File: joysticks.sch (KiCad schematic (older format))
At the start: 31 parts, among them CN4 JOY1, CN5 JOY2, U11 74LS125

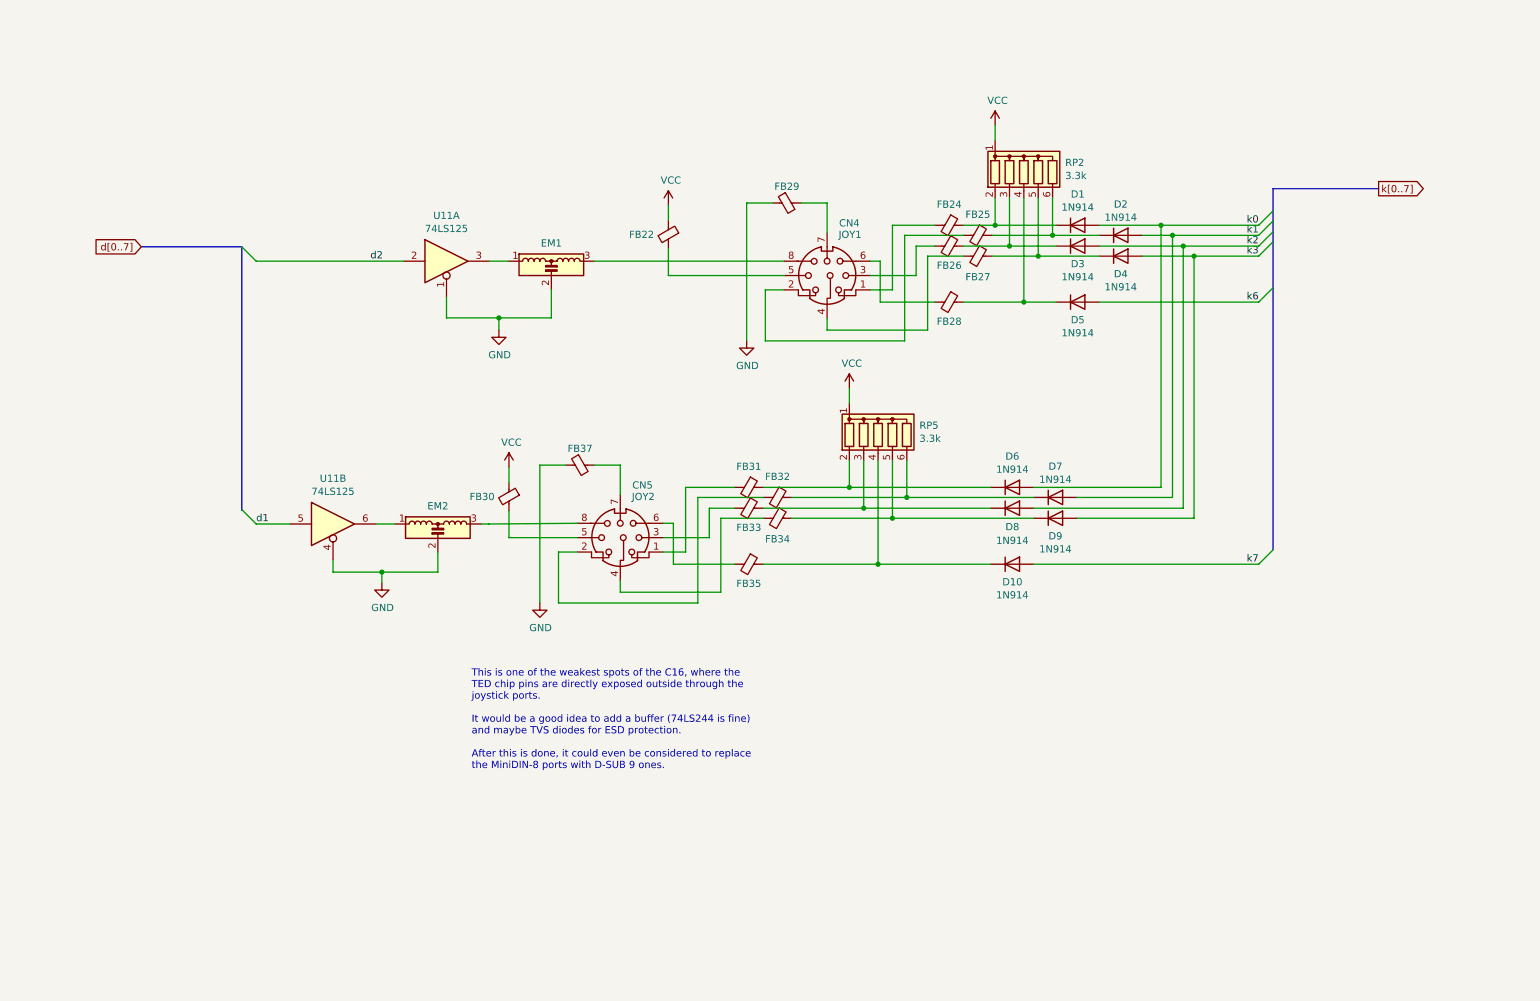
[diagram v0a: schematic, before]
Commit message: Add buffers on joystick ports - WIP
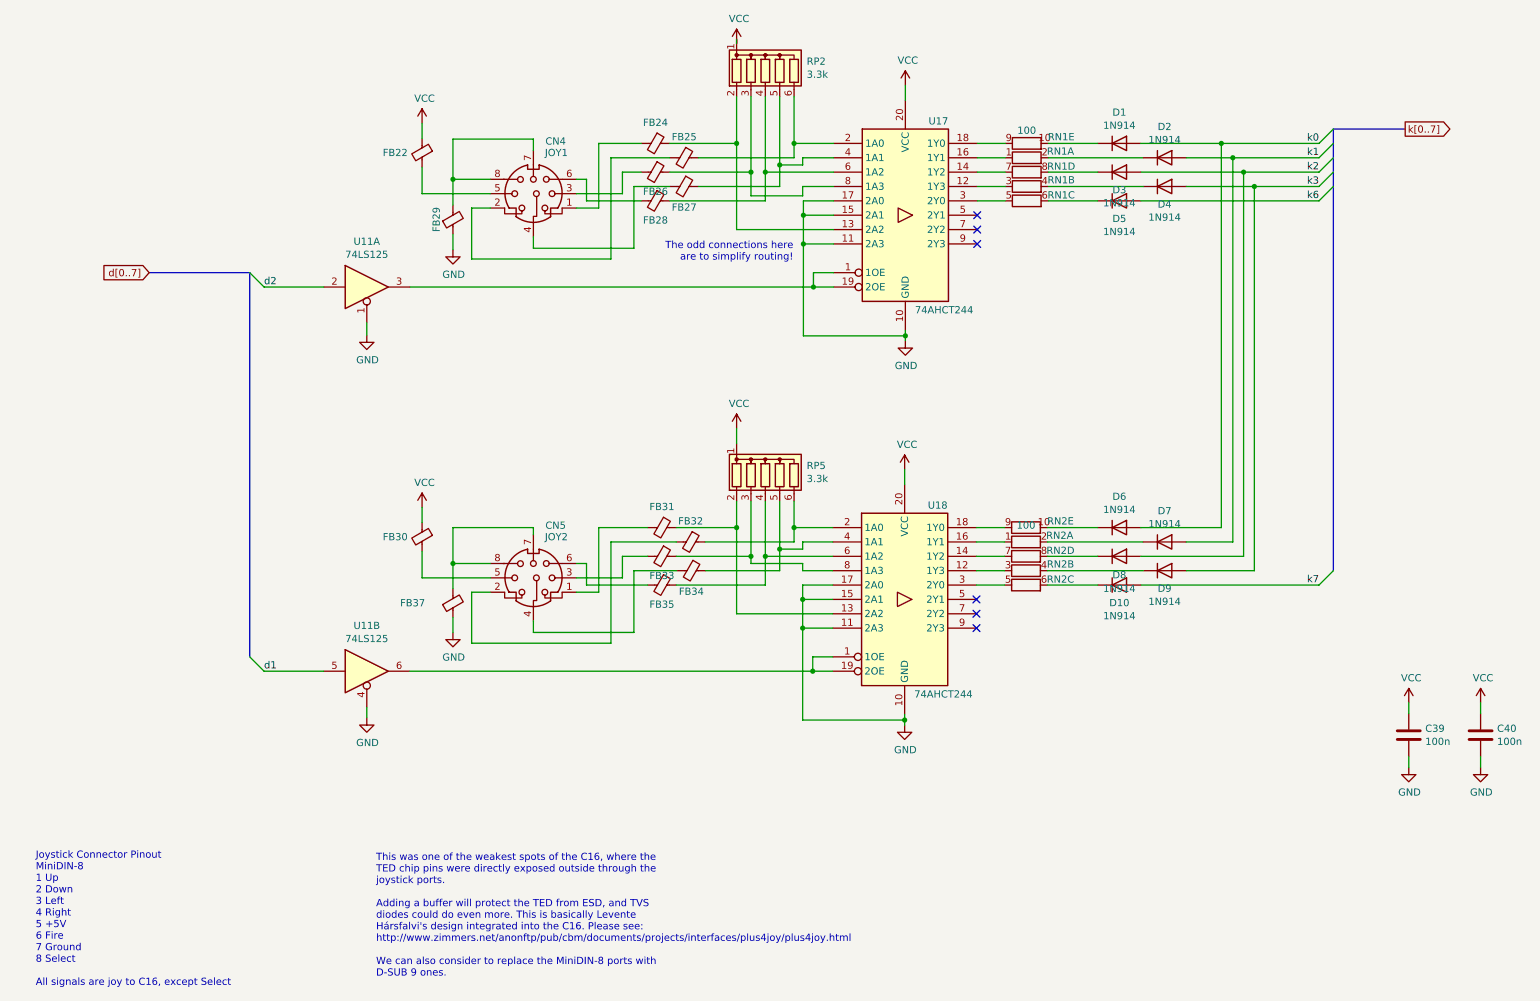
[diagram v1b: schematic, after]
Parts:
- removed EM1, EM2: EMI_Filter_LCL, LittleSixteen:EMI_Filter, symbol Device:EMI_Filter_LCL
- added C39, C40: 100n, Capacitor_THT:C_Disc_D8.0mm_W2.5mm_P5.00mm, symbol Device:C
- added RN1, RN2: 100, Resistor_THT:R_Array_SIP10, symbol Device:R_Pack05_SIP_Split
- added U17, U18: 74AHCT244, Package_DIP:DIP-20_W7.62mm_Socket_LongPads, symbol 74xx:74AHCT244
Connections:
- net GND: now also C39.2, C40.2, U17.10 (GND), U17.11 (2A3), U17.15 (2A1), U17.17 (2A0), U18.10 (GND), U18.11 (2A3), U18.15 (2A1), U18.17 (2A0)
- net VCC: now also C39.1, C40.1, U17.20 (VCC), U18.20 (VCC)
- net at CN4.7, FB29.2: now also CN4.8
- net at U11.3: now also U17.1 (1OE), U17.19 (2OE)
- net at FB24.1, RP2.2 (R1): now also U17.13 (2A2); no longer D1.1 (K)
- net at FB25.1, RP2.6 (R5): now also U17.2 (1A0); no longer D2.1 (K)
- net at FB26.1, RP2.3 (R2): now also U17.8 (1A3); no longer D3.1 (K)
- net at FB27.1, RP2.5 (R4): now also U17.4 (1A1); no longer D4.1 (K)
- net at FB28.1, RP2.4 (R3): now also U17.6 (1A2); no longer D5.1 (K)
- net at U11.6: now also U18.1 (1OE), U18.19 (2OE)
- net at CN5.8: now also CN5.7, FB37.2
- net at FB31.1, RP5.2 (R1): now also U18.13 (2A2); no longer D6.1 (K)
- net at FB32.1, RP5.6 (R5): now also U18.2 (1A0); no longer D7.1 (K)
- net at FB33.1, RP5.3 (R2): now also U18.8 (1A3); no longer D8.1 (K)
- net at FB34.1, RP5.5 (R4): now also U18.4 (1A1); no longer D9.1 (K)
- net at FB35.1, RP5.4 (R3): now also U18.6 (1A2); no longer D10.1 (K)
- new net: D1.1 (K), RN1.10 (R5.2)
- new net: D2.1 (K), RN1.2 (R1.2)
- new net: D3.1 (K), RN1.8 (R4.2)
- new net: D4.1 (K), RN1.4 (R2.2)
- new net: D5.1 (K), RN1.6 (R3.2)
- new net: D6.1 (K), RN2.10 (R5.2)
- new net: D7.1 (K), RN2.2 (R1.2)
- new net: D8.1 (K), RN2.8 (R4.2)
- new net: D9.1 (K), RN2.4 (R2.2)
- new net: D10.1 (K), RN2.6 (R3.2)
- new net: RN2.3 (R2.1), U18.12 (1Y3)
- new net: RN2.7 (R4.1), U18.14 (1Y2)
- new net: RN2.1 (R1.1), U18.16 (1Y1)
- new net: RN2.9 (R5.1), U18.18 (1Y0)
- new net: RN2.5 (R3.1), U18.3 (2Y0)
- new net: RN1.3 (R2.1), U17.12 (1Y3)
- new net: RN1.7 (R4.1), U17.14 (1Y2)
- new net: RN1.1 (R1.1), U17.16 (1Y1)
- new net: RN1.9 (R5.1), U17.18 (1Y0)
- new net: RN1.5 (R3.1), U17.3 (2Y0)
- no-connect marks 0 -> 6
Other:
- note added: "Joystick Connector Pinout\nMiniDIN-8\n1 Up\n2 Down\n3 Left\n4 Right\n5 +5V\n6 Fire\n7 Ground\n8 Select\n\nAll signals are joy to C16, except Select"
- note added: "The odd connections here\nare to simplify routing!"
- note added: "This was one of the weakest spots of the C16, where the\nTED chip pins were directly exposed outside through the\njoystick ports.\n\nAdding a buffer will protect the TED from ESD, and TVS\ndiodes could do even more. This is basically Levente\nHársfalvi's design integrated into the C16. Please see:\nhttp://www.zimmers.net/anonftp/pub/cbm/documents/projects/interfaces/plus4joy/plus4joy.html\n\nWe c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"
- note removed: "This is one of the weakest spots of the C16, where the\nTED chip pins are directly exposed outside through the\njoystick ports.\n\nIt would be a good idea to add a buffer (74LS244 is fine)\nand maybe TVS diodes for ESD protection.\n\nAfter this is done, it could even be considered to replace\nthe MiniDIN-8 ports with D-SUB 9 ones."
- moved on the sheet: CN4, CN5, D1, D10, D2, D3, D4, D5, D6, D7, D8, D9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

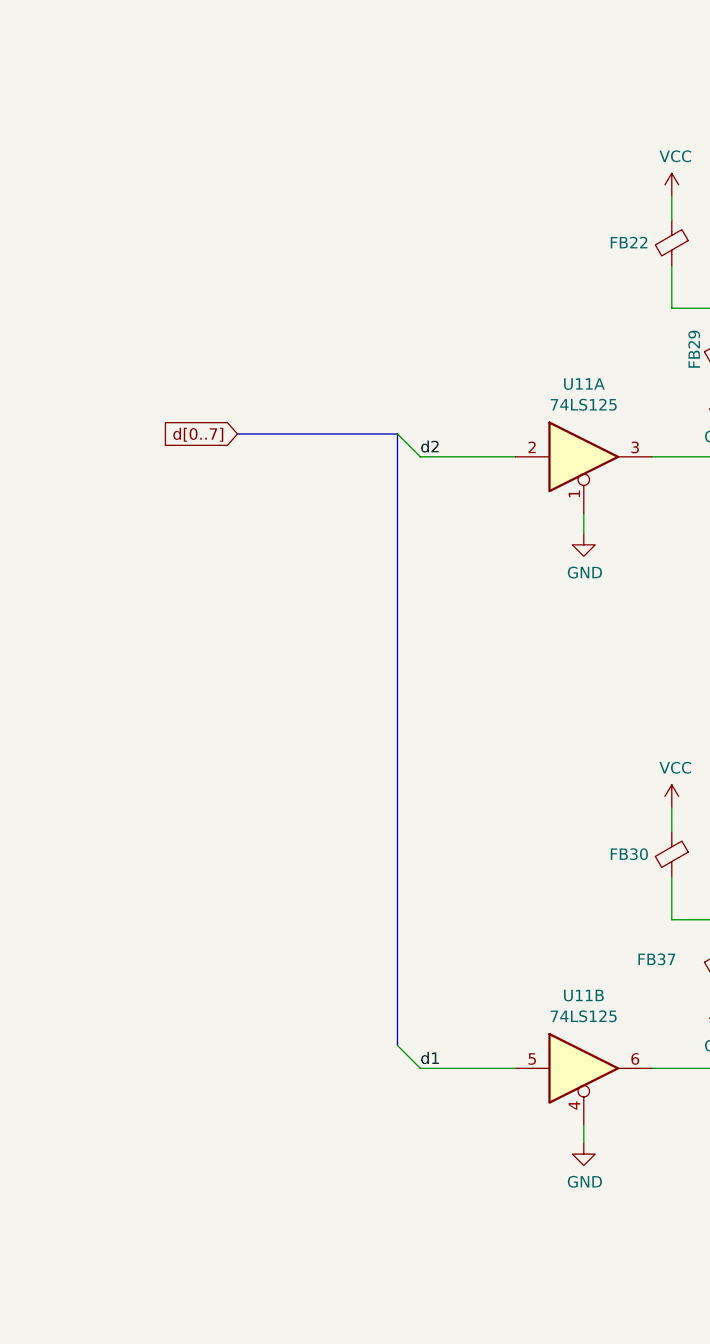
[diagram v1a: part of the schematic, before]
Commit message: Restore JD1/2
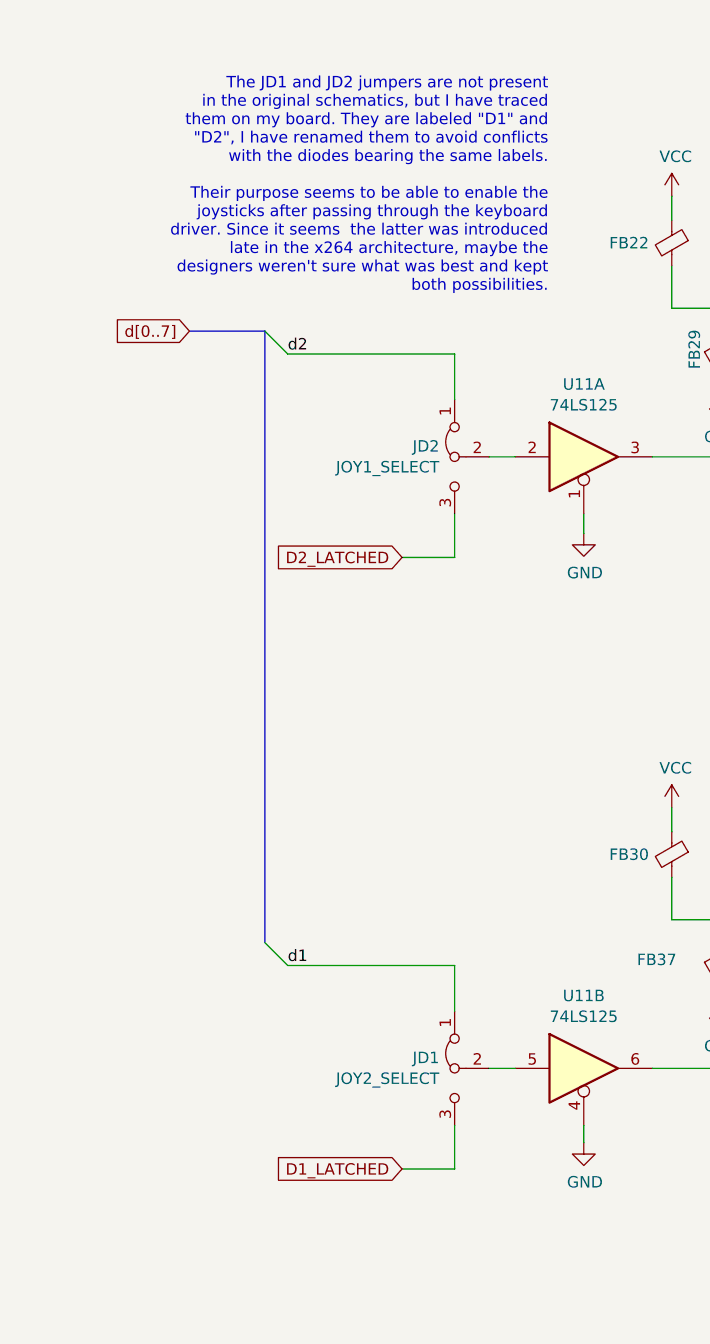
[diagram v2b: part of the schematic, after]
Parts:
- added JD1: JOY2_SELECT, LittleSixteen:SolderJumper2x, symbol Jumper:Jumper_3_Bridged12
- added JD2: JOY1_SELECT, LittleSixteen:SolderJumper2x, symbol Jumper:Jumper_3_Bridged12
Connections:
- net d1: now also JD1.1 (A); no longer U11.5
- net d2: now also JD2.1 (A); no longer U11.2
- new net: JD2.2 (C), U11.2
- new net: JD1.2 (C), U11.5
- new net D1_LATCHED: JD1.3 (B)
- new net D2_LATCHED: JD2.3 (B)
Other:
- note added: "The JD1 and JD2 jumpers are not present\nin the original schematics, but I have traced\nthem on my board. They are labeled "D1" and\n"D2", I have renamed them to avoid conflicts\nwith the diodes bearing the same labels.\n\nTheir purpose seems to be able to enable the\njoysticks after passing through the keyboard\ndriver. Since it seems the latter was introduced\nlate in the x264 architecture, may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"
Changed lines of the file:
@@
 Sheet 11 12
 Title "LittleSixteen"
-Date "2021-11-03"
+Date "2021-11-06"
 Rev "3git"
 Comp "SukkoPera"
@@
 	3255 5480 6060 5480
 Wire Wire Line
-	2240 2805 2655 2805
-Wire Wire Line
 	2955 3055 2955 3140
 Wire Wire Line
 	2955 5730 2955 5805
-Text Label 2240 5480 0    50   ~ 0
+Text Label 1660 5030 0    50   ~ 0
 d1
 Wire Wire Line
-	2240 5480 2655 5480
+	2540 5480 2655 5480
 $Comp
 L 74xx:74LS125 U11
@@
 	1    0    0    -1
 $EndComp
-Text GLabel 1440 2705 0    50   Input ~ 0
+Text GLabel 1230 2255 0    50   Input ~ 0
 d[0..7]
 Wire Bus Line
-	1440 2705 2140 2705
+	1230 2255 1560 2255
 Entry Wire Line
-	2140 5380 2240 5480
+	1560 4930 1660 5030
 Entry Wire Line
-	2140 2705 2240 2805
+	1560 2255 1660 2355
 $Comp
 L 74xx:74LS125 U11
@@
 	1    0    0    -1
 $EndComp
-Text Label 2240 2805 0    50   ~ 0
+Text Label 1660 2355 0    50   ~ 0
 d2
 Wire Wire Line
@@
 	6065 2805 6205 2805
 Wire Bus Line
-	2140 2705 2140 5380
+	1560 2255 1560 4930
 Wire Wire Line
 	10710 6075 10710 6150
@@
 Wire Wire Line
 	5995 3145 6705 3145
-Wire Bus Line
-	9685 1705 9685 4780
 Connection ~ 6705 3145
 Wire Wire Line
@@
 Text Notes 5925 2630 2    50   ~ 0
 The odd connections here\nare to simplify routing!
+$Comp
+L Jumper:Jumper_3_Bridged12 JD1
+U 1 1 61F59301
+P 2390 5480
+F 0 "JD1" V 2344 5547 50  0000 L CNN
+F 1 "JOY2_SELECT" V 2435 5547 50  0000 L CNN
+F 2 "LittleSixteen:SolderJumper2x" H 2390 5480 50  0001 C CNN
+F 3 "~" H 2390 5480 50  0001 C CNN
+	1    2390 5480
+	0    -1   1    0
+$EndComp
+Wire Wire Line
+	2390 5730 2390 5920
+Wire Wire Line
+	2390 5920 2160 5920
+Text GLabel 2160 5920 0    50   Input ~ 0
+D1_LATCHED
+Wire Wire Line
+	2540 2805 2655 2805
+$Comp
+L Jumper:Jumper_3_Bridged12 JD2
+U 1 1 61F9FE8A
+P 2390 2805
+F 0 "JD2" V 2344 2872 50  0000 L CNN
+F 1 "JOY1_SELECT" V 2435 2872 50  0000 L CNN
+F 2 "LittleSixteen:SolderJumper2x" H 2390 2805 50  0001 C CNN
+F 3 "~" H 2390 2805 50  0001 C CNN
+	1    2390 2805
+	0    -1   1    0
+$EndComp
+Wire Wire Line
+	2390 3055 2390 3245
+Wire Wire Line
+	2390 3245 2160 3245
+Text GLabel 2160 3245 0    50   Input ~ 0
+D2_LATCHED
+Wire Wire Line
+	2390 2355 2390 2555
+Wire Wire Line
+	1660 2355 2390 2355
+Wire Wire Line
+	2390 5030 2390 5230
+Wire Wire Line
+	1660 5030 2390 5030
+Wire Bus Line
+	9685 1705 9685 4780
+Text Notes 2800 2090 2    50   ~ 0
+The JD1 and JD2 jumpers are not present\nin the original schematics, but I have traced\nthem on my board. They are labeled "D1" and\n"D2", I have renamed them to avoid conflicts\nwith the diodes bearing the same labels.\n\nTheir purpose seems to be able to enable the\njoysticks after passing through the keyboard\ndriver. Since it seems  the latter was introduced\nlate in the x264 architecture, maybe the\ndesigners weren't sure what was best and kept\nboth possibilities.
 $EndSCHEMATC

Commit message: Switch to Kycon MiniDIN connectors
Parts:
- removed CN4: JOY1, LittleSixteen:Connector_Mini-DIN_Female_8Pin_2rows, symbol Connector:Mini-DIN-8
- removed CN5: JOY2, LittleSixteen:Connector_Mini-DIN_Female_8Pin_2rows, symbol Connector:Mini-DIN-8
- added CN4: JOY1, LittleSixteen:KMDGX-8S-BS, symbol mini-din-8:Mini-DIN-8
- added CN5: JOY2, LittleSixteen:KMDGX-8S-BS, symbol mini-din-8:Mini-DIN-8
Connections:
- net GND: now also CN4.0 (SH), CN5.0 (SH)
- net at FB24.2: now also CN4.1
- net at FB25.2: now also CN4.2
- net at FB26.2: now also CN4.3
- net at FB27.2: now also CN4.4
- net at FB22.2: now also CN4.5
- net at FB28.2: now also CN4.6
- net at FB29.2: now also CN4.7, CN4.8
- net at FB31.2: now also CN5.1
- net at FB32.2: now also CN5.2
- net at FB33.2: now also CN5.3
- net at FB34.2: now also CN5.4
- net at FB30.2: now also CN5.5
- net at FB35.2: now also CN5.6
- net at FB37.2: now also CN5.7, CN5.8
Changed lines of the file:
@@
 $EndComp
-Wire Wire Line
-	4815 4780 4815 5210
 Wire Wire Line
 	4735 4680 4910 4680
@@
 	4415 4730 4485 4730
 Wire Wire Line
-	4115 5210 4815 5210
-Wire Wire Line
-	4115 5130 4115 5210
-Wire Wire Line
 	4735 4830 4735 4680
 Wire Wire Line
@@
 Wire Wire Line
 	4415 4930 4570 4930
-$Comp
-L Connector:Mini-DIN-8 CN5
-U 1 1 5E19A816
-P 4115 4830
-F 0 "CN5" H 4270 5195 50  0000 C CNN
-F 1 "JOY2" H 4275 5115 50  0000 C CNN
-F 2 "LittleSixteen:Connector_Mini-DIN_Female_8Pin_2rows" V 4105 4820 50  0001 C CNN
-F 3 "http://service.powerdynamics.com/ec/Catalog17/Section%2011.pdf" V 4105 4820 50  0001 C CNN
-	1    4115 4830
-	1    0    0    -1
-$EndComp
 $Comp
 L power:GND #PWR0109
@@
 $EndComp
 Wire Wire Line
-	4815 2105 4815 2535
+	4815 2105 4815 2355
 Wire Wire Line
 	4735 2005 4865 2005
@@
 	4415 2055 4485 2055
 Wire Wire Line
-	4115 2535 4815 2535
-Wire Wire Line
-	4115 2455 4115 2535
-Wire Wire Line
 	4735 2155 4735 2005
 Wire Wire Line
@@
 Wire Wire Line
 	4415 2255 4570 2255
-$Comp
-L Connector:Mini-DIN-8 CN4
-U 1 1 5DF69658
-P 4115 2155
-F 0 "CN4" H 4270 2520 50  0000 C CNN
-F 1 "JOY1" H 4275 2440 50  0000 C CNN
-F 2 "LittleSixteen:Connector_Mini-DIN_Female_8Pin_2rows" V 4105 2145 50  0001 C CNN
-F 3 "http://service.powerdynamics.com/ec/Catalog17/Section%2011.pdf" V 4105 2145 50  0001 C CNN
-	1    4115 2155
-	1    0    0    -1
-$EndComp
 Entry Wire Line
 	9585 1805 9685 1705
@@
 	8345 4880 9585 4880
 Wire Wire Line
-	3555 5105 3555 5210
+	3555 5105 3555 5160
 Wire Wire Line
 	3555 4480 4115 4480
@@
 $EndComp
 Wire Wire Line
-	3555 2435 3555 2545
+	3555 2435 3555 2490
 Wire Wire Line
 	5930 1480 5930 1805
@@
 Wire Wire Line
 	1660 5030 2390 5030
+Text Notes 2800 2090 2    50   ~ 0
+The JD1 and JD2 jumpers are not present\nin the original schematics, but I have traced\nthem on my board. They are labeled "D1" and\n"D2", I have renamed them to avoid conflicts\nwith the diodes bearing the same labels.\n\nTheir purpose seems to be able to enable the\njoysticks after passing through the keyboard\ndriver. Since it seems  the latter was introduced\nlate in the x264 architecture, maybe the\ndesigners weren't sure what was best and kept\nboth possibilities.
+$Comp
+L mini-din-8:Mini-DIN-8 CN5
+U 1 1 62150BCE
+P 4115 4830
+F 0 "CN5" H 4320 5150 50  0000 C CNN
+F 1 "JOY2" H 4315 5075 50  0000 C CNN
+F 2 "LittleSixteen:KMDGX-8S-BS" V 4105 4820 50  0001 C CNN
+F 3 "http://service.powerdynamics.com/ec/Catalog17/Section%2011.pdf" V 4105 4820 50  0001 C CNN
+	1    4115 4830
+	1    0    0    -1
+$EndComp
+Wire Wire Line
+	4415 5030 4815 5030
+Wire Wire Line
+	4815 4780 4815 5030
+Wire Wire Line
+	4115 5160 3555 5160
+Wire Wire Line
+	4115 5130 4115 5160
+Connection ~ 3555 5160
+Wire Wire Line
+	3555 5160 3555 5210
+$Comp
+L mini-din-8:Mini-DIN-8 CN4
+U 1 1 62179774
+P 4115 2155
+F 0 "CN4" H 4295 2485 50  0000 C CNN
+F 1 "JOY1" H 4295 2410 50  0000 C CNN
+F 2 "LittleSixteen:KMDGX-8S-BS" V 4105 2145 50  0001 C CNN
+F 3 "http://service.powerdynamics.com/ec/Catalog17/Section%2011.pdf" V 4105 2145 50  0001 C CNN
+	1    4115 2155
+	1    0    0    -1
+$EndComp
+Wire Wire Line
+	4415 2355 4815 2355
+Wire Wire Line
+	3555 2490 4115 2490
+Wire Wire Line
+	4115 2490 4115 2455
 Wire Bus Line
 	9685 1705 9685 4780
-Text Notes 2800 2090 2    50   ~ 0
-The JD1 and JD2 jumpers are not present\nin the original schematics, but I have traced\nthem on my board. They are labeled "D1" and\n"D2", I have renamed them to avoid conflicts\nwith the diodes bearing the same labels.\n\nTheir purpose seems to be able to enable the\njoysticks after passing through the keyboard\ndriver. Since it seems  the latter was introduced\nlate in the x264 architecture, maybe the\ndesigners weren't sure what was best and kept\nboth possibilities.
+Connection ~ 3555 2490
+Wire Wire Line
+	3555 2490 3555 2545
 $EndSCHEMATC
